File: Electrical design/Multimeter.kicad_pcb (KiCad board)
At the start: 2 copper layers, 90 x 130 mm, 194 parts, among them P101 Expansion header, P102 Programming header, P103 Mounting hole, P104 Mounting hole, P105 Mounting hole, P201 10 A, P202 mA, P203 V R, P204 COMMON, P401 CONN_01X01, P402 CONN_01X01, P403 CONN_01X01, P404 CONN_01X01, P405 CONN_01X01, P406 CONN_01X05, P407 CONN_01X05, P501 USB_OTG, Q101 Q_PMOS_GSD, Q102 Q_NMOS_GSD, Q201 Q_NMOS_GSD, Q301 Q_PMOS_GSD, Q302 Q_NMOS_GSD, Q501 Q_NMOS_GSD, Q502 Q_PMOS_GSD, SW401 SW_PUSH, U101 STM32F373R8Tx, U102 ILI9341_LCD_Breakout, U103 BD4835, U201 CT138, U202 MCP6002, U203 MCP6N11, U204 74LVC1G66 GNDA, U205 CT138, U206 74LVC1G66 GNDA, U207 TSV634, U208 74LVC1G66 GNDA, U209 74LVC1G66 GNDA, U210 74LVC1G66 GNDA, U211 74LVC1G66 GNDA, U212 74LVC1G66 GNDA, U213 74LVC1G66 GNDA, U214 74LVC1G66 GNDA, U215 74LVC1G66 GNDA, U216 74LVC1G66 GNDA, U217 74LVC1G66 GNDA, U218 74LVC1G66 GNDA, U301 NCV551SN33T1G, U302 MAX6070, U501 TPD2E001, U502 MCP73834, Y101 8 MHz

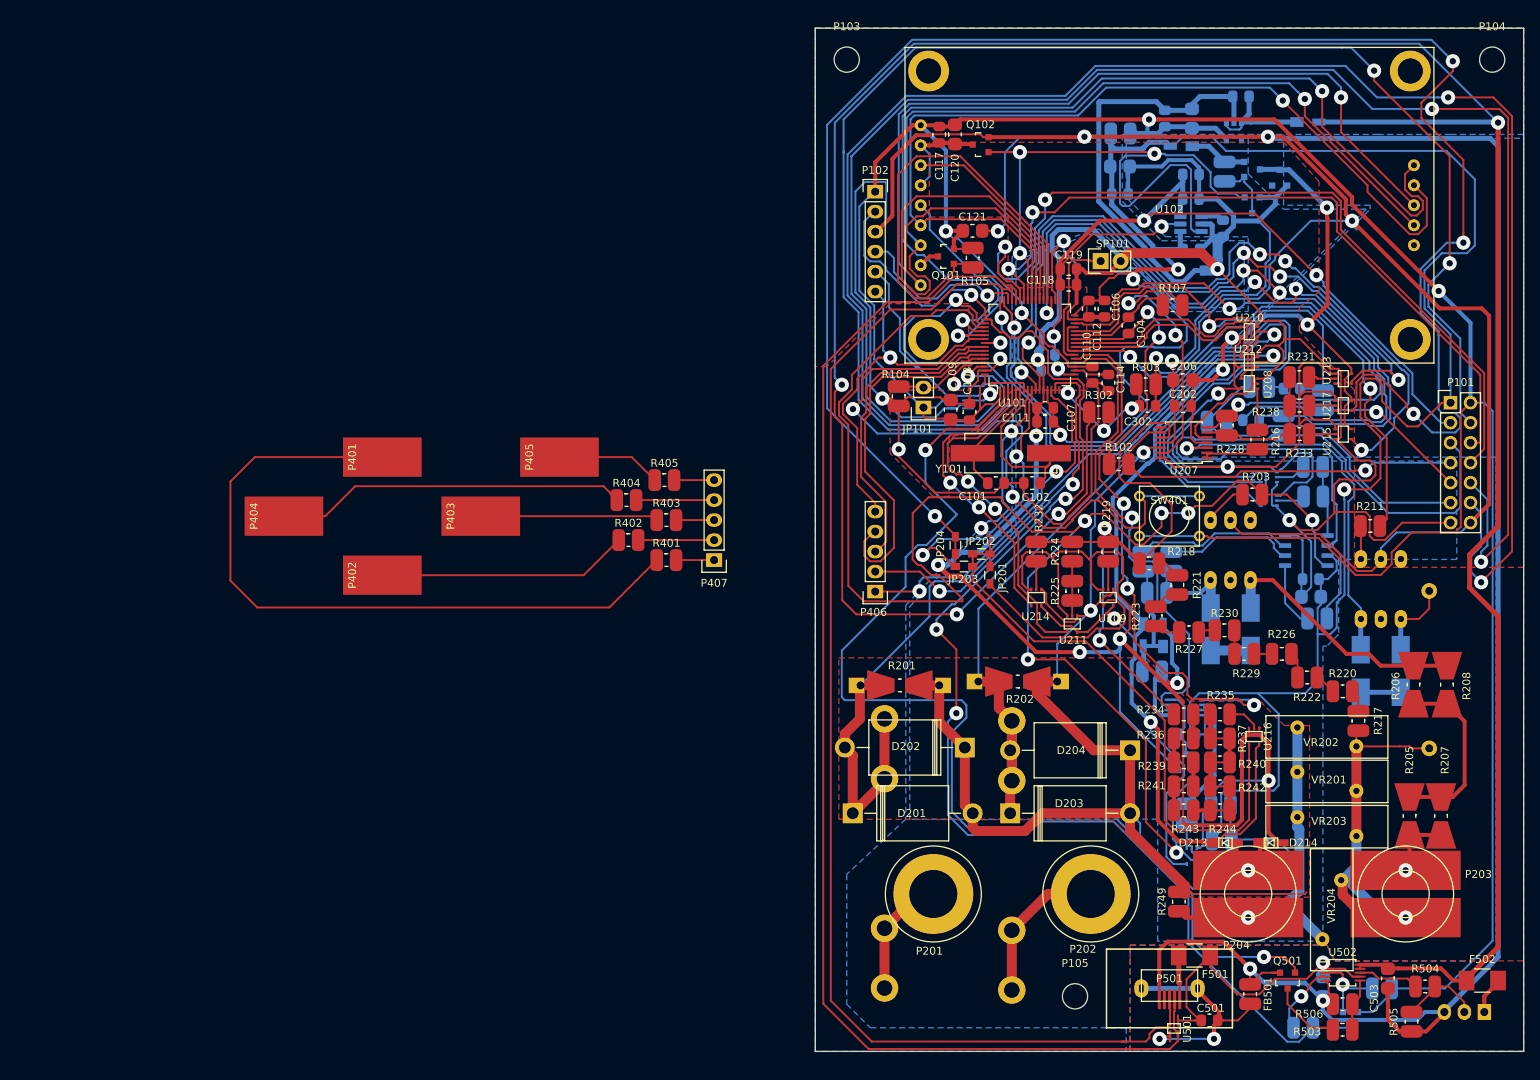
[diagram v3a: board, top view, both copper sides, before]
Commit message: Fix current circuit connection, PCB layout.
The current measurement circuit has to connect directly to the Common terminal!
The PCB layout had traces going between the pads of the Common terminal, where
there's actually a non-plated hole. I've updated the footprint to include the hole,
although unfortunately that produces about 20 DRC errors, and also re-routed stuff.
Also updated the value of D301 to match a real Zener diode.
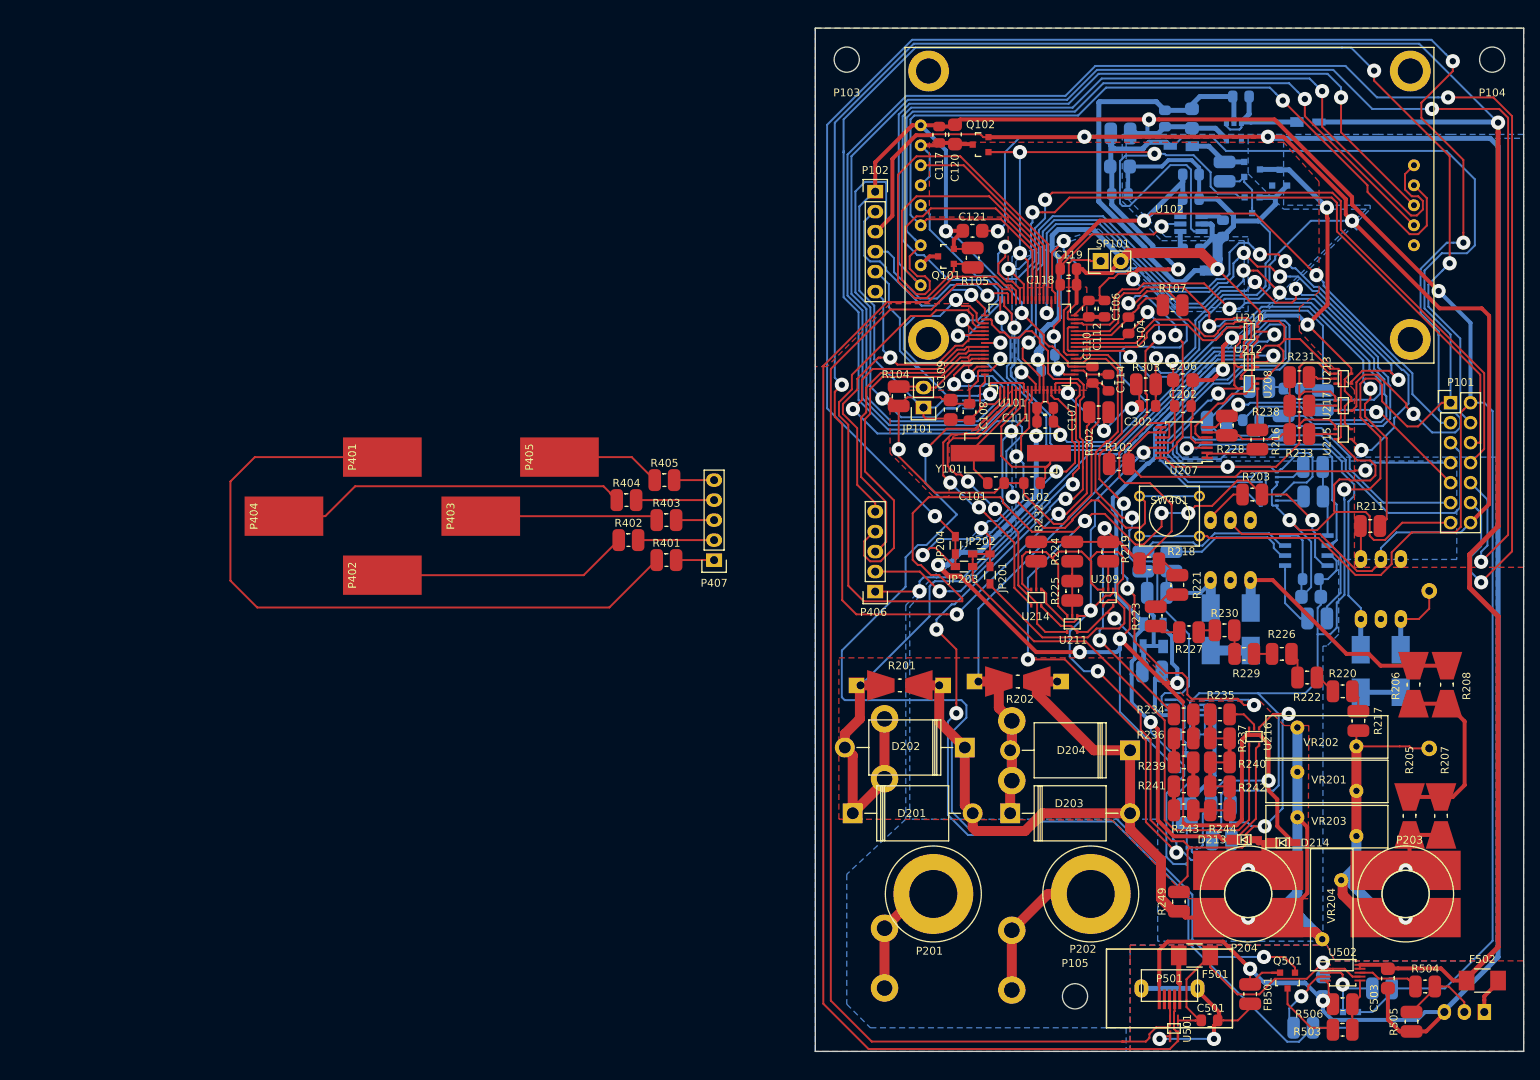
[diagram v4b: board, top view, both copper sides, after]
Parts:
- D301: value 3.5V -> 3.6V
- moved D213 2.43 mm to (194.5, 129.1)
- moved D214 1.50 mm to (199.4, 129.5)
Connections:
- D201 pad 2: /Main Input / Output/COM -> /Main Input / Output/COM_D
- D202 pad 1: /Main Input / Output/COM -> /Main Input / Output/COM_D
- D203 pad 2: /Main Input / Output/COM -> /Main Input / Output/COM_D
- D204 pad 1: /Main Input / Output/COM -> /Main Input / Output/COM_D
- P204 pad 1: Net-(P204-Pad1) -> /Main Input / Output/COM_D
- R201 pad 1: /Main Input / Output/COM -> /Main Input / Output/COM_D
- R202 pad 1: /Main Input / Output/COM -> /Main Input / Output/COM_D
- R249 pad 1: Net-(P204-Pad1) -> /Main Input / Output/COM_D
- VR201 pad 2: Net-(P204-Pad1) -> /Main Input / Output/COM_D
- VR202 pad 2: Net-(P204-Pad1) -> /Main Input / Output/COM_D
- VR203 pad 2: Net-(P204-Pad1) -> /Main Input / Output/COM_D
- VR204 pad 2: Net-(P204-Pad1) -> /Main Input / Output/COM_D
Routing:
- net /Main Input / Output/COM_D: track 0.00 -> 168.5 mm, vias 0 -> 1
- net /Main Input / Output/COM: track 194.6 -> 125.8 mm, vias 2 -> 5
- net Net-(P204-Pad1): track 53.5 -> 0.00 mm, vias 1 -> 0
- net Net-(D213-Pad2): track 20.3 -> 18.5 mm
- added copper zone on F.Cu, net /Main Input / Output/COM_D
- removed copper zone on F.Cu, net /Main Input / Output/COM

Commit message: Connect the reset circuit to +BATT so that it actually works!
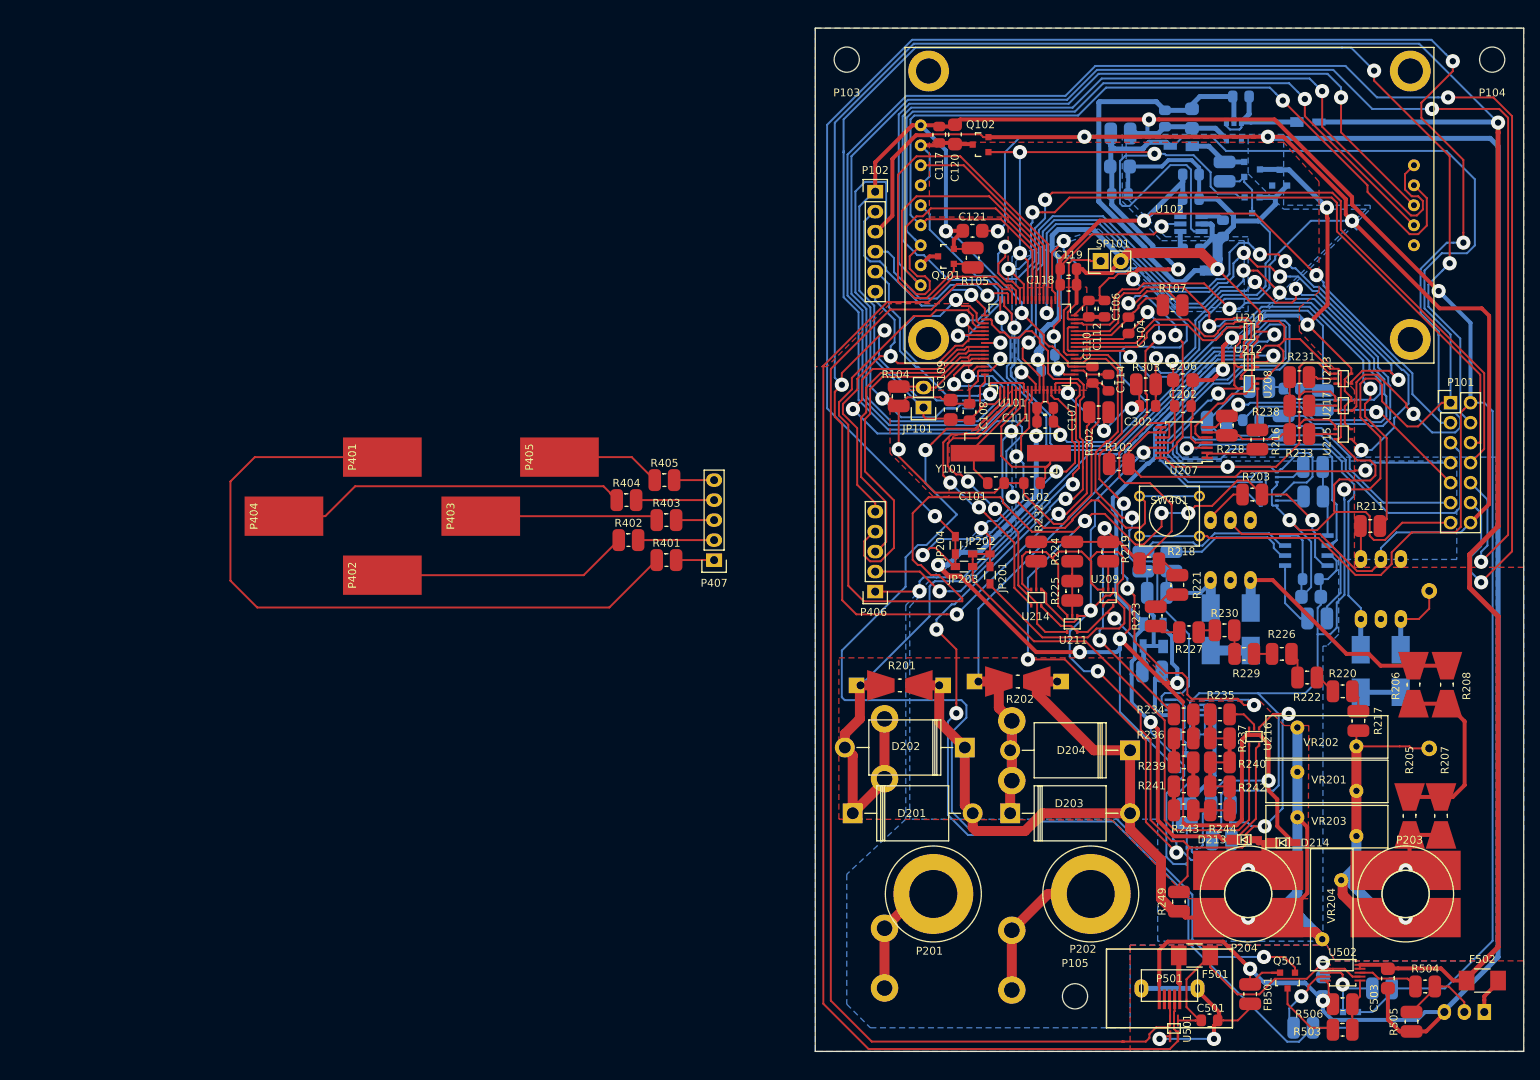
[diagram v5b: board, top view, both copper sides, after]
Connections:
- U103 pad 5: +3V3 -> +BATT
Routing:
- net +BATT: track 354.3 -> 378.9 mm, vias 4 -> 5
- net +3V3: track 378.5 -> 374.5 mm

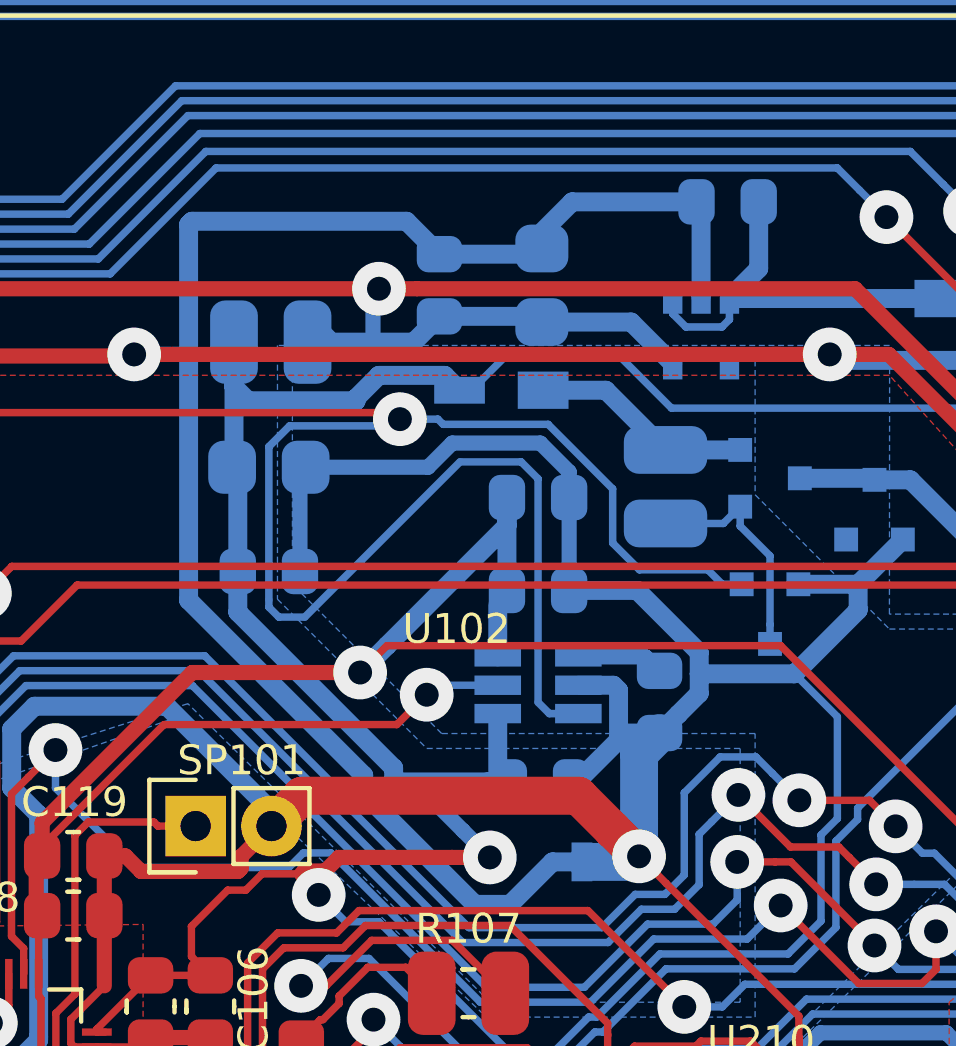
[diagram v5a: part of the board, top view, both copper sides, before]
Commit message: Add the analog switch schematic component to the cache. Some PCB layout tweaks.
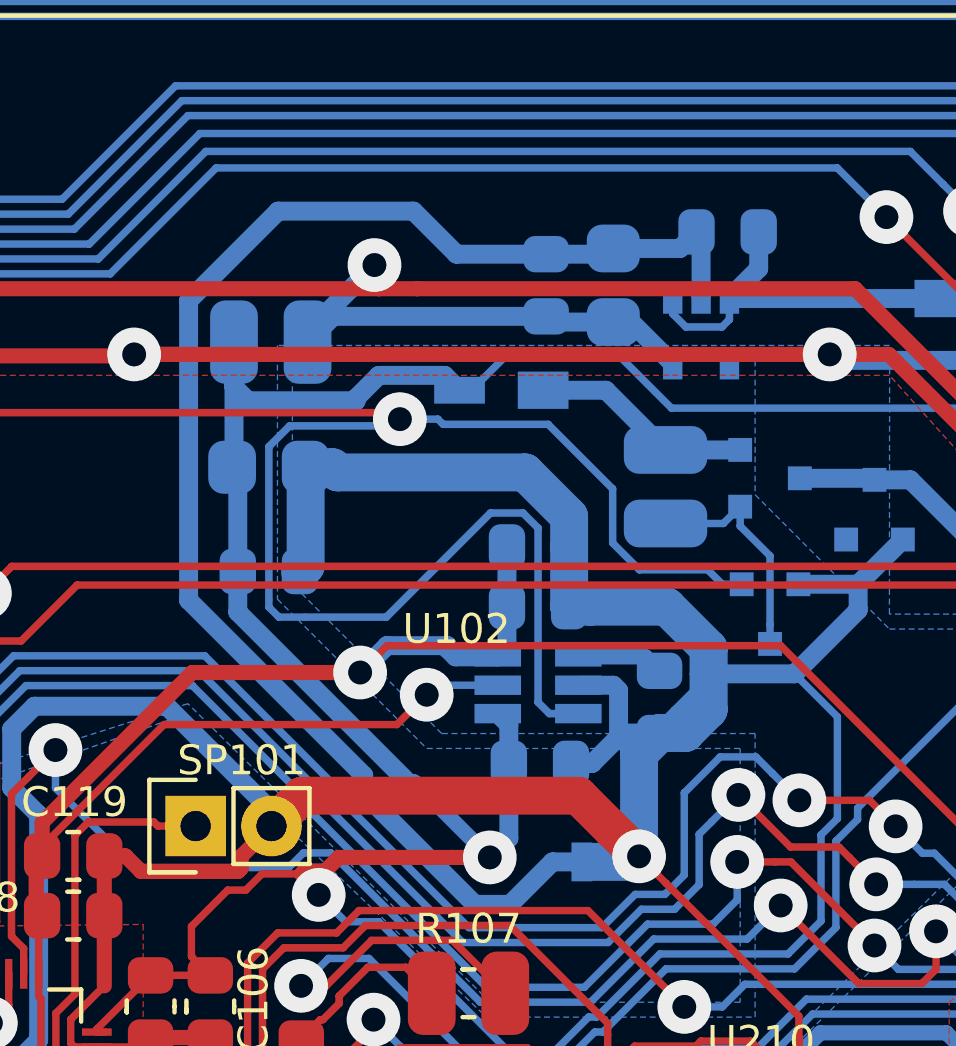
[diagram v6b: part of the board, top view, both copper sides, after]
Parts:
- moved C303 3.57 mm to (188.0, 37.5)
- moved C304 2.39 mm to (190.2, 37.5)
- moved C309 1.65 mm to (187.7, 46.2)
- moved C301 1.01 mm to (194.1, 35.7)
- moved C307 0.62 mm to (187.8, 53.5)
- moved C308 0.54 mm to (187.7, 48.2)
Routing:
- net GNDA: track 492.8 -> 499.9 mm
- net +Vref: track 113.9 -> 110.1 mm
- net /PS_EN: track 89.9 -> 87.5 mm
- net GNDD: track 639.7 -> 637.5 mm
- net Net-(C301-Pad1): track 14.1 -> 13.1 mm
- net +3.3VA: track 306.0 -> 305.2 mm
- net +3V3: track 374.5 -> 375.2 mm
